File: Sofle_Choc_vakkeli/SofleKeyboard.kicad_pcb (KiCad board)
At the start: 2 copper layers, 162.7 x 111.8 mm, 96 parts, among them J2 4PIN, J3 OLED, P1 i2c_pin, P2 i2c_pin, SW1 SW_PUSH_LED, SW10 SW_PUSH_LED, SW11 SW_PUSH_LED, SW12 SW_PUSH_LED, SW13 SW_PUSH_LED, SW14 SW_PUSH_LED, SW15 SW_PUSH_LED, SW16 SW_PUSH_LED, SW17 SW_PUSH_LED, SW18 SW_PUSH_LED, SW19 SW_PUSH_LED, SW2 SW_PUSH_LED, SW20 SW_PUSH_LED, SW21 SW_PUSH_LED, SW22 SW_PUSH_LED, SW23 SW_PUSH_LED, SW24 SW_PUSH_LED, SW25 Rotary_Encoder_Switch, SW26 SW_PUSH_LED, SW27 SW_PUSH_LED, SW28 SW_PUSH_LED, SW29 SW_PUSH_LED, SW3 SW_PUSH_LED, SW30 SW_PUSH_LED, SW31 SW_PUSH_LED, SW32 SW_PUSH_LED, SW33 SW_PUSH_LED, SW34 SW_PUSH_LED, SW35 SW_PUSH_LED, SW4 SW_PUSH_LED, SW5 SW_PUSH_LED, SW6 SW_PUSH_LED, SW7 SW_PUSH_LED, SW8 SW_PUSH_LED, SW9 SW_PUSH_LED, U1 ProMicro

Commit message: fixes, stabs, breakaways
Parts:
- removed the TH6 at (234.7, 48.9)
- removed the TH6 at (235.4, 114.6)
- added REF**: breakaway-hole, Keebio-Parts:breakaway-hole, F.Cu at (235.2, 118.2)
- added REF**: breakaway-hole, Keebio-Parts:breakaway-hole, F.Cu at (225.5, 87.7)
- added REF**: breakaway-hole, Keebio-Parts:breakaway-hole, F.Cu at (225.5, 86.7)
- added REF**: breakaway-hole, Keebio-Parts:breakaway-hole, F.Cu at (225.5, 84.6)
- added REF**: breakaway-hole, Keebio-Parts:breakaway-hole, F.Cu at (225.5, 54.7)
- added REF**: breakaway-hole, Keebio-Parts:breakaway-hole, F.Cu at (225.5, 55.7)
- added REF**: breakaway-hole, Keebio-Parts:breakaway-hole, F.Cu at (225.5, 56.7)
- added REF**: breakaway-hole, Keebio-Parts:breakaway-hole, F.Cu at (225.5, 57.7)
- added REF**: breakaway-hole, Keebio-Parts:breakaway-hole, F.Cu at (225.5, 58.7)
- added REF**: breakaway-hole, Keebio-Parts:breakaway-hole, F.Cu at (225.5, 48.6)
- added REF**: breakaway-hole, Keebio-Parts:breakaway-hole, F.Cu at (225.5, 47.5)
- added REF**: breakaway-hole, Keebio-Parts:breakaway-hole, F.Cu at (242.5, 118.2)
- added REF**: breakaway-hole, Keebio-Parts:breakaway-hole, F.Cu at (225.5, 46.5)
- added REF**: breakaway-hole, Keebio-Parts:breakaway-hole, F.Cu at (244.1, 118.2)
- added REF**: breakaway-hole, Keebio-Parts:breakaway-hole, F.Cu at (225.5, 130.6)
- added REF**: breakaway-hole, Keebio-Parts:breakaway-hole, F.Cu at (225.5, 132.1)
- added REF**: breakaway-hole, Keebio-Parts:breakaway-hole, F.Cu at (225.5, 133.4)
- added REF**: breakaway-hole, Keebio-Parts:breakaway-hole, F.Cu at (225.5, 123.0)
- added REF**: breakaway-hole, Keebio-Parts:breakaway-hole, F.Cu at (225.5, 121.5)
- added REF**: breakaway-hole, Keebio-Parts:breakaway-hole, F.Cu at (225.5, 120.4)
- added STAB1: STAB, SofleChoc:Kailh-PG1350-2u-stab, F.Cu at (234.8, 100.0)
- added STAB2: STAB, SofleChoc:Kailh-PG1350-2u-stab, F.Cu at (234.8, 61.9)
- added TH6: HOLE, SofleKeyboard-footprint:HOLE_M2_TH, F.Cu at (235.7, 81.1)
- added TH6: HOLE, SofleKeyboard-footprint:HOLE_M2_TH, F.Cu at (239.2, 117.9)
- moved D33 4.62 mm to (227.0, 122.0), turned to 270 degrees
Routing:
- net col6: track 421.3 -> 448.1 mm
- net row2: track 206.6 -> 219.8 mm
- net GND: track 1119.5 -> 1127.1 mm, vias 55 -> 67
- net Net-(D33-Pad2): track 28.3 -> 20.8 mm
- net VCC: track 1030.6 -> 1032.6 mm
- net Net-(D32-Pad2): track 30.7 -> 32.6 mm
- net Net-(SW32-Pad2): track 39.8 -> 40.9 mm
- net col0: track 339.1 -> 339.5 mm, vias 7 -> 8
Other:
- outline, holes or cut-outs redrawn
- board text added: "Sofle Choc ISO by Vakkeli"
- board text removed: "Sofle Choc v2.1 by Brian Low"

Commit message: fixed single breakable button gnd, added dxf for 3d.
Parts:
- removed TH1, TH2: HOLE, SofleKeyboard-footprint:M2_HOLE_PCB
- added J1: PimorioniTrackball, Keebio-Parts:pimoroni_trackball, F.Cu at (108.5, 94.0)
- added JP10: Jumper_NO_Small, SofleKeyboard-footprint:Jumper, F.Cu at (106.4, 91.4)
- added JP12: Solder if this side up!, SofleKeyboard-footprint:Jumper, F.Cu at (106.1, 83.8)
- added JP13: Solder if this side up, SofleKeyboard-footprint:Jumper, B.Cu at (106.4, 94.0)
- added JP15: Jumper_NO_Small, SofleKeyboard-footprint:Jumper, B.Cu at (106.2, 86.4)
- added JP16: Jumper_NO_Small, SofleKeyboard-footprint:Jumper, B.Cu at (106.2, 83.8)
- added JP9: Jumper_NO_Small, SofleKeyboard-footprint:Jumper, F.Cu at (106.4, 94.0)
- added SW3: Rotary_Encoder_Switch, SofleChoc:EVQWGD001, F.Cu at (101.6, 106.7)
- JP7: value Jumper_NO_Small -> Solder if this side up!
- moved R1 41.4 mm to (98.5, 38.9), turned to 180 degrees
- moved R2 37.3 mm to (89.9, 41.7), turned to 270 degrees
- moved RSW1 7.12 mm to (93.7, 83.6), turned to 90 degrees
- moved J2 6.05 mm to (88.1, 91.7)
- moved P2 5.79 mm to (108.5, 77.5)
- moved P1 5.77 mm to (108.5, 80.0)
- moved SW25 5.15 mm to (97.0, 108.7)
- moved D25 1.99 mm to (106.2, 98.8), turned to 180 degrees
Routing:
- net GND: track 1127.1 -> 1073.8 mm, vias 67 -> 72
- net ENCB: track 73.9 -> 126.5 mm, vias 1 -> 0
- net ENCA: track 69.0 -> 96.4 mm, vias 1 -> 0
- net SCL: track 49.6 -> 75.4 mm
- net SDA: track 57.5 -> 82.3 mm, vias 4 -> 5
- net SW25B: track 7.11 -> 26.7 mm, vias 1 -> 0
- net VCC: track 1032.6 -> 1051.4 mm, vias 43 -> 46
- net SW25A: track 201.0 -> 214.4 mm
- net /i2c_d: track 29.6 -> 39.8 mm
- net /i2c_c: track 9.85 -> 18.7 mm
- net (no net): track 0.00 -> 5.29 mm
- net Net-(J1-Pad5): track 0.00 -> 3.66 mm
- net Net-(J1-Pad1): track 0.00 -> 3.11 mm
- net RESET: track 51.2 -> 48.5 mm, vias 0 -> 1
- net row4: track 210.9 -> 208.6 mm, vias 9 -> 8
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
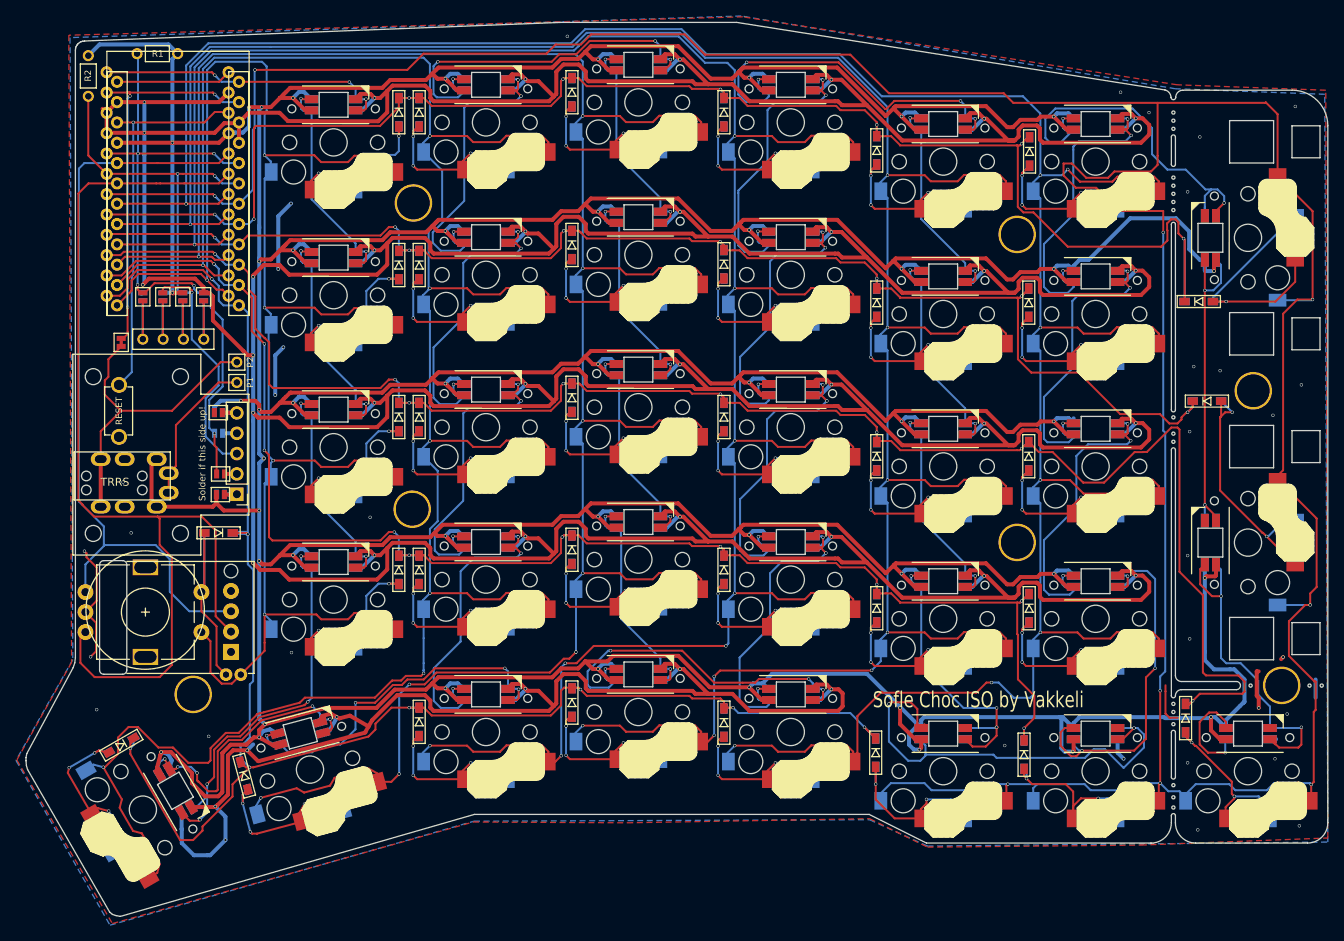
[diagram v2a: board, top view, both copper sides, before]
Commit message: fixed single button led order
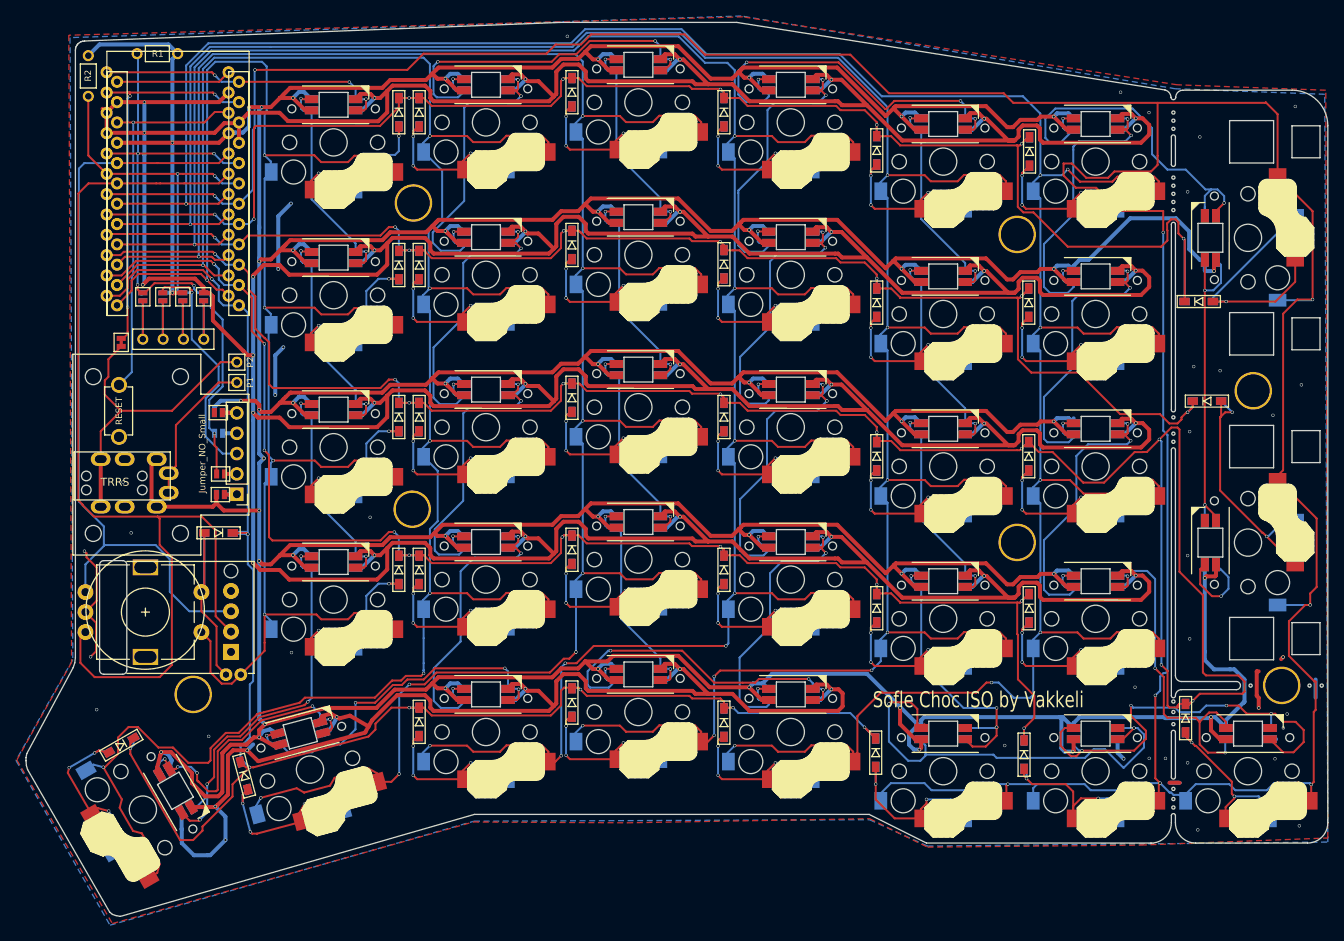
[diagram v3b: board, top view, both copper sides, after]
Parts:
- removed the REF** at (225.5, 130.6)
- removed the REF** at (225.5, 132.1)
- removed the REF** at (225.5, 120.4)
- added REF**: breakaway-hole, Keebio-Parts:breakaway-hole, F.Cu at (225.5, 131.1)
- added REF**: breakaway-hole, Keebio-Parts:breakaway-hole, F.Cu at (225.5, 132.3)
- added REF**: breakaway-hole, Keebio-Parts:breakaway-hole, F.Cu at (225.5, 120.1)
- JP12, JP7: value Solder if this side up! -> Jumper_NO_Small
- JP13: value Solder if this side up -> Jumper_NO_Small
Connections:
- SW33 pad 2: Net-(SW33-Pad2) -> Net-(SW24-Pad4)
- SW33 pad 4: Net-(SW32-Pad2) -> Net-(SW33-Pad4)
- SW34 pad 2: Net-(SW24-Pad4) -> Net-(SW33-Pad4)
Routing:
- net Net-(SW33-Pad4): track 0.00 -> 55.0 mm, vias 0 -> 4
- net row2: track 219.8 -> 256.2 mm, vias 8 -> 10
- net Net-(SW32-Pad2): track 40.9 -> 10.9 mm, vias 2 -> 1
- net Net-(SW33-Pad2): track 13.0 -> 0.00 mm, vias 1 -> 0
- net (no net): track 5.29 -> 0.00 mm
- net Net-(SW24-Pad4): track 46.7 -> 43.7 mm
- net GND: track 1073.8 -> 1076.3 mm, vias 72 -> 76
- net col6: track 448.1 -> 449.2 mm

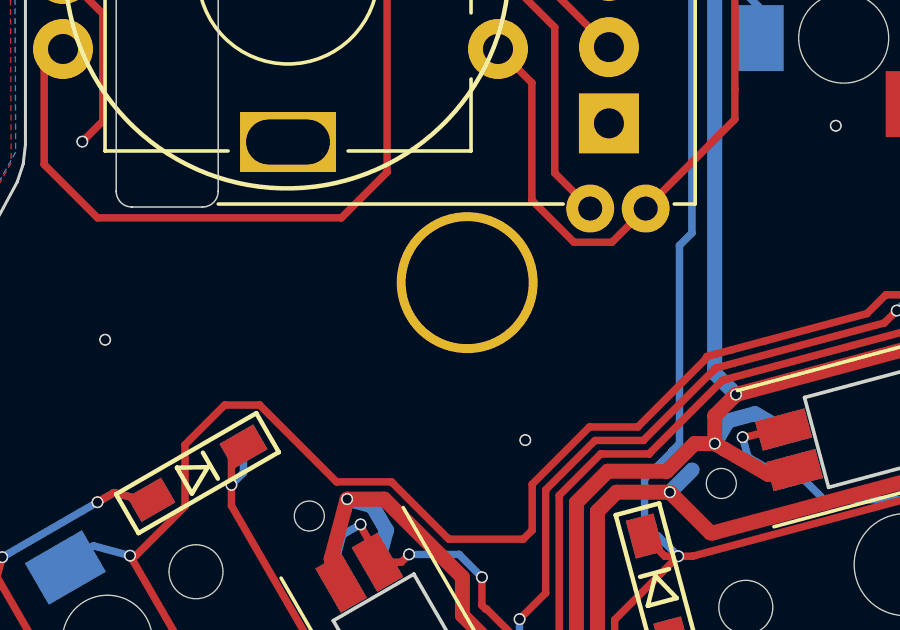
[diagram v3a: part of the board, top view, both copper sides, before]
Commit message: Fixes to pcb. Added functioning, but incomplete fw
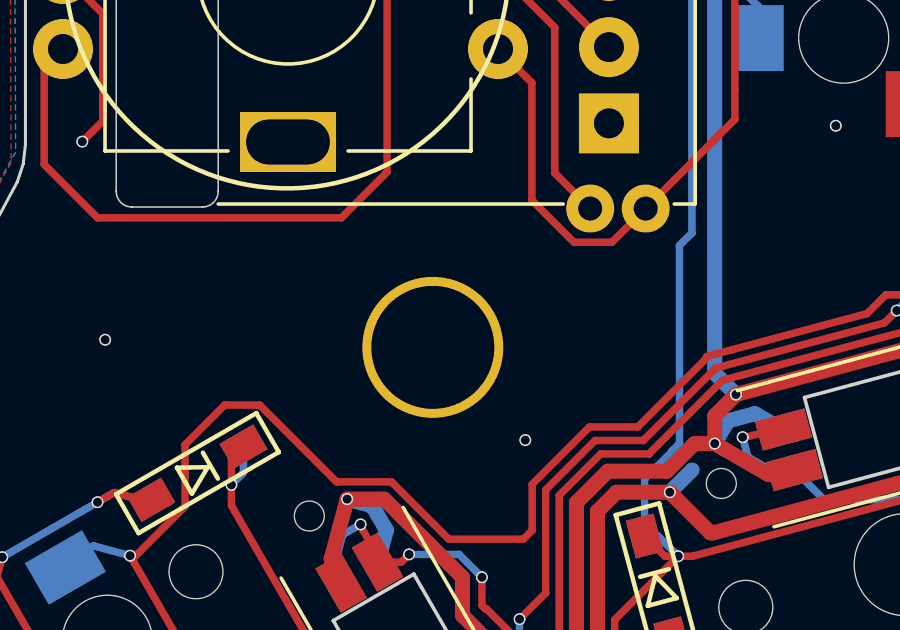
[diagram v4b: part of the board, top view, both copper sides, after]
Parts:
- moved TH7 2.44 mm to (101.9, 121.2)
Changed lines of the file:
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@@
     (visible_elements 7EFFFEFF)
     (pcbplotparams
-      (layerselection 0x010f0_7ffffffe)
+      (layerselection 0x010f0_ffffffff)
       (usegerberextensions true)
       (usegerberattributes false)
@@
       (padsonsilk false)
       (subtractmaskfromsilk true)
-      (outputformat 3)
+      (outputformat 1)
       (mirror false)
       (drillshape 0)
@@
   )
   (module SofleKeyboard-footprint:HOLE_M2_TH (layer F.Cu)
-    (at 103 119 90)
+    (at 101.854 121.158 90)
     (fp_text reference TH7 (at 0 -2.54 90) (layer F.SilkS) hide
       (effects (font (size 0.29972 0.29972) (thickness 0.0762)))
